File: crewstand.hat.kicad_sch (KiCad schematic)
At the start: 20 parts, among them J1 GPIO, J2 CAN Terminal, J3 Sensor Terminal, J4 V-In, J5 Screw_Terminal_01x08, J6 V-Out, J7 Relais2, J8 Relais1, J9 V-Out, U2 MCP2515-xSO, U3 MCP2551-I-P, U4 PicoW, Y2 12M

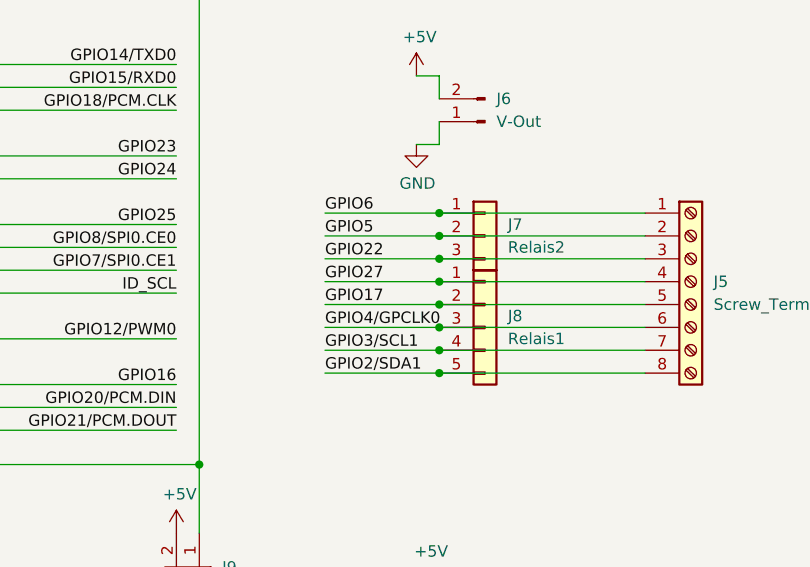
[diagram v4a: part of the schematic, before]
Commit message: fix(relais-gpio): use GPIO26 & 19
- GPIO 2&3 where high on boot
- ensures all pins are low until actively switched by backend
- minor changes on routing and footprints

issue #13
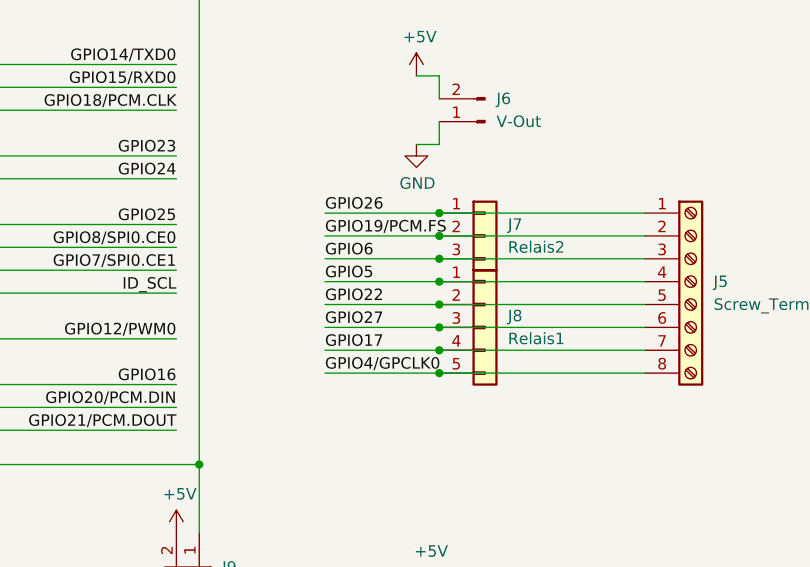
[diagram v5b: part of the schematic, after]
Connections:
- net GPIO17: now also J5.7 (Pin_7), J8.4 (Pin_4); no longer J5.5 (Pin_5), J8.2 (Pin_2)
- net GPIO19/PCM.FS: now also J5.2 (Pin_2), J7.2 (Pin_2)
- net GPIO22: now also J5.5 (Pin_5), J8.2 (Pin_2); no longer J5.3 (Pin_3), J7.3 (Pin_3)
- net GPIO26: now also J5.1 (Pin_1), J7.1 (Pin_1)
- net GPIO27: now also J5.6 (Pin_6), J8.3 (Pin_3); no longer J5.4 (Pin_4), J8.1 (Pin_1)
- net GPIO2/SDA1: no longer J5.8 (Pin_8), J8.5 (Pin_5)
- net GPIO3/SCL1: no longer J5.7 (Pin_7), J8.4 (Pin_4)
- net GPIO4/GPCLK0: now also J5.8 (Pin_8), J8.5 (Pin_5); no longer J5.6 (Pin_6), J8.3 (Pin_3)
- net GPIO5: now also J5.4 (Pin_4), J8.1 (Pin_1); no longer J5.2 (Pin_2), J7.2 (Pin_2)
- net GPIO6: now also J5.3 (Pin_3), J7.3 (Pin_3); no longer J5.1 (Pin_1), J7.1 (Pin_1)
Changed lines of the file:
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@@
     (effects (font (size 1.27 1.27)) (justify left bottom))
   )
-  (label "GPIO4{slash}GPCLK0" (at 116.84 64.77 0) (fields_autoplaced)
+  (label "GPIO4{slash}GPCLK0" (at 116.84 69.85 0) (fields_autoplaced)
     (effects (font (size 1.27 1.27)) (justify left bottom))
   )
-  (label "GPIO3{slash}SCL1" (at 116.84 67.31 0) (fields_autoplaced)
-    (effects (font (size 1.27 1.27)) (justify left bottom))
-  )
-  (label "GPIO27" (at 116.84 59.69 0) (fields_autoplaced)
+  (label "GPIO27" (at 116.84 64.77 0) (fields_autoplaced)
     (effects (font (size 1.27 1.27)) (justify left bottom))
   )
@@
     (effects (font (size 1.27 1.27)) (justify right bottom))
   )
-  (label "GPIO17" (at 116.84 62.23 0) (fields_autoplaced)
+  (label "GPIO17" (at 116.84 67.31 0) (fields_autoplaced)
     (effects (font (size 1.27 1.27)) (justify left bottom))
   )
@@
     (effects (font (size 1.27 1.27)) (justify left bottom))
   )
-  (label "GPIO2{slash}SDA1" (at 116.84 69.85 0) (fields_autoplaced)
-    (effects (font (size 1.27 1.27)) (justify left bottom))
-  )
   (label "GPIO23" (at 100.33 45.72 180) (fields_autoplaced)
     (effects (font (size 1.27 1.27)) (justify right bottom))
@@
   (label "GPIO15{slash}RXD0" (at 100.33 38.1 180) (fields_autoplaced)
     (effects (font (size 1.27 1.27)) (justify right bottom))
+  )
+  (label "GPIO19{slash}PCM.FS" (at 116.84 54.61 0) (fields_autoplaced)
+    (effects (font (size 1.27 1.27)) (justify left bottom))
   )
   (label "GPIO16" (at 100.33 71.12 180) (fields_autoplaced)
@@
     (effects (font (size 1.27 1.27)) (justify left bottom))
   )
-  (label "GPIO6" (at 116.84 52.07 0) (fields_autoplaced)
+  (label "GPIO6" (at 116.84 57.15 0) (fields_autoplaced)
     (effects (font (size 1.27 1.27)) (justify left bottom))
   )
@@
     (effects (font (size 1.27 1.27)) (justify right bottom))
   )
-  (label "GPIO5" (at 116.84 54.61 0) (fields_autoplaced)
+  (label "GPIO5" (at 116.84 59.69 0) (fields_autoplaced)
     (effects (font (size 1.27 1.27)) (justify left bottom))
   )
@@
     (effects (font (size 1.27 1.27)) (justify right bottom))
   )
-  (label "GPIO22" (at 116.84 57.15 0) (fields_autoplaced)
+  (label "GPIO26" (at 116.84 52.07 0) (fields_autoplaced)
     (effects (font (size 1.27 1.27)) (justify left bottom))
   )
+  (label "GPIO22" (at 116.84 62.23 0) (fields_autoplaced)
+    (effects (font (size 1.27 1.27)) (justify left bottom))
+  )
